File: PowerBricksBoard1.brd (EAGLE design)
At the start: 76.2 x 50.8 mm, 11 parts

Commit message: Board with draft routing
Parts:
- turned R1 to 270 degrees
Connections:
- net 12V renamed G
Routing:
- net ON/OFF: track 0.00 -> 58.2 mm
- net DATA: track 0.00 -> 31.6 mm
- net ALERT: track 0.00 -> 31.3 mm
- net CLK: track 0.00 -> 25.5 mm
- net G: track 0.00 -> 11.8 mm
- net 12_GND: track 0.00 -> 11.6 mm
- net N$1: track 0.00 -> 4.11 mm
- added copper zone on layer 1, net 12_GND
- added copper zone on layer 16, net 12_GND
- added copper zone on layer 16, net 48V
- added copper zone on layer 16, net 48_GND
- added copper zone on layer 1, net G
- added copper zone on layer 16, net G

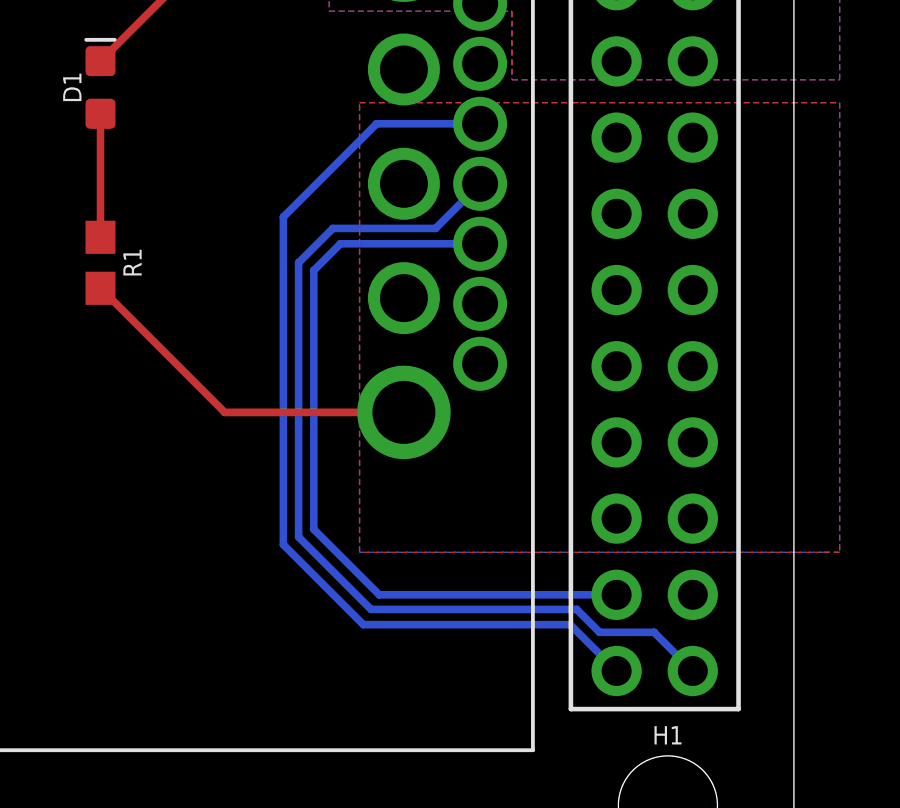
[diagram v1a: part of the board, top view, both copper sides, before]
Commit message: Fixed DRC error
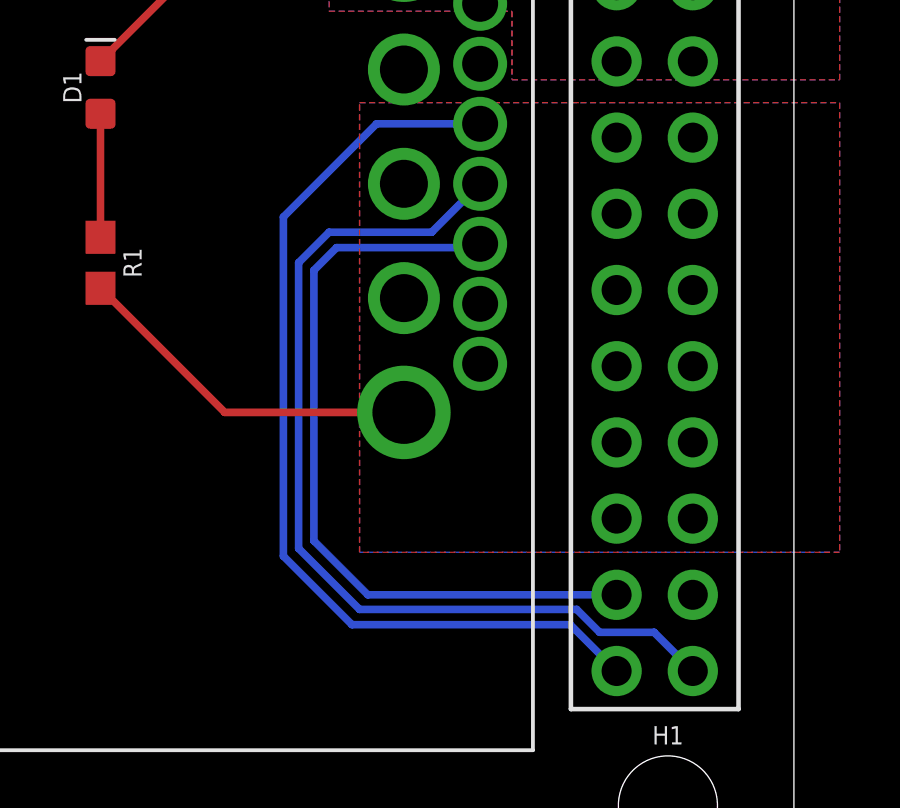
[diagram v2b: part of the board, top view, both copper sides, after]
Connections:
- removed net N$14: U$5.53
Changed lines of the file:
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@@
 <setting verticaltext="up"/>
 </settings>
-<grid distance="10" unitdist="mil" unit="mil" style="lines" multiple="1" display="yes" altdistance="5" altunitdist="mil" altunit="mil"/>
+<grid distance="5" unitdist="mil" unit="mil" style="lines" multiple="1" display="yes" altdistance="5" altunitdist="mil" altunit="mil"/>
 <layers>
 <layer number="1" name="Top" color="4" fill="1" visible="yes" active="yes"/>
@@
 </class>
 </classes>
-<designrules name="default">
+<designrules name="ECE_Senior_Design">
 <description language="de">&lt;b&gt;EAGLE Design Rules&lt;/b&gt;
 &lt;p&gt;
@@
 Einstellungen hier und speichern die Design Rules unter
 einem neuen Namen ab.</description>
-<description language="en">&lt;b&gt;EAGLE Design Rules&lt;/b&gt;
+<description language="en">&lt;b&gt;ECE 402/477 Design Rules Version 2&lt;/b&gt;
 &lt;p&gt;
-The default Design Rules have been set to cover
-a wide range of applications. Your particular design
-may have different requirements, so please make the
-necessary adjustments and save your customized
-design rules under a new name.</description>
+These are the design rules to use for Purdue University electrical and computer engineering senior design PCBs.
+&lt;/p&gt;
+&lt;p&gt;
+Please make sure your boards conform to these design rules.
+&lt;/p&gt;
+</description>
 <param name="layerSetup" value="(1*16)"/>
-<param name="mtCopper" value="0.035mm 0.035mm 0.035mm 0.035mm 0.035mm 0.035mm 0.035mm 0.035mm 0.035mm 0.035mm 0.035mm 0.035mm 0.035mm 0.035mm 0.035mm 0.035mm"/>
-<param name="mtIsolate" value="1.5mm 0.15mm 0.2mm 0.15mm 0.2mm 0.15mm 0.2mm 0.15mm 0.2mm 0.15mm 0.2mm 0.15mm 0.2mm 0.15mm 0.2mm"/>
-<param name="mdWireWire" value="6mil"/>
-<param name="mdWirePad" value="6mil"/>
-<param name="mdWireVia" value="6mil"/>
+<param name="mtCopper" value="0.0356mm 0.0356mm 0.0356mm 0.0356mm 0.0356mm 0.0356mm 0.0356mm 0.0356mm 0.0356mm 0.0356mm 0.0356mm 0.0356mm 0.0356mm 0.0356mm 0.0356mm 0.0356mm"/>
+<param name="mtIsolate" value="1.5011mm 0.1499mm 0.2007mm 0.1499mm 0.2007mm 0.1499mm 0.2007mm 0.1499mm 0.2007mm 0.1499mm 0.2007mm 0.1499mm 0.2007mm 0.1499mm 0.2007mm"/>
+<param name="mdWireWire" value="8mil"/>
+<param name="mdWirePad" value="8mil"/>
+<param name="mdWireVia" value="8mil"/>
 <param name="mdPadPad" value="6mil"/>
-<param name="mdPadVia" value="6mil"/>
-<param name="mdViaVia" value="6mil"/>
+<param name="mdPadVia" value="8mil"/>
+<param name="mdViaVia" value="8mil"/>
 <param name="mdSmdPad" value="6mil"/>
 <param name="mdSmdVia" value="6mil"/>
 <param name="mdSmdSmd" value="6mil"/>
-<param name="mdViaViaSameLayer" value="6mil"/>
+<param name="mdViaViaSameLayer" value="8mil"/>
 <param name="mnLayersViaInSmd" value="2"/>
-<param name="mdCopperDimension" value="40mil"/>
-<param name="mdDrill" value="6mil"/>
+<param name="mdCopperDimension" value="15mil"/>
+<param name="mdDrill" value="8mil"/>
 <param name="mdSmdStop" value="0mil"/>
-<param name="msWidth" value="6mil"/>
-<param name="msDrill" value="0.35mm"/>
-<param name="msMicroVia" value="9.99mm"/>
+<param name="msWidth" value="8mil"/>
+<param name="msDrill" value="13mil"/>
+<param name="msMicroVia" value="13mil"/>
 <param name="msBlindViaRatio" value="0.5"/>
 <param name="rvPadTop" value="0.25"/>
@@
 <param name="rvMicroViaOuter" value="0.25"/>
 <param name="rvMicroViaInner" value="0.25"/>
-<param name="rlMinPadTop" value="10mil"/>
+<param name="rlMinPadTop" value="7mil"/>
 <param name="rlMaxPadTop" value="20mil"/>
-<param name="rlMinPadInner" value="10mil"/>
+<param name="rlMinPadInner" value="7mil"/>
 <param name="rlMaxPadInner" value="20mil"/>
-<param name="rlMinPadBottom" value="10mil"/>
+<param name="rlMinPadBottom" value="7mil"/>
 <param name="rlMaxPadBottom" value="20mil"/>
-<param name="rlMinViaOuter" value="8mil"/>
+<param name="rlMinViaOuter" value="7mil"/>
 <param name="rlMaxViaOuter" value="20mil"/>
-<param name="rlMinViaInner" value="8mil"/>
+<param name="rlMinViaInner" value="7mil"/>
 <param name="rlMaxViaInner" value="20mil"/>
 <param name="rlMinMicroViaOuter" value="4mil"/>
@@
 <param name="mvStopFrame" value="1"/>
 <param name="mvCreamFrame" value="0"/>
-<param name="mlMinStopFrame" value="4mil"/>
-<param name="mlMaxStopFrame" value="4mil"/>
+<param name="mlMinStopFrame" value="3mil"/>
+<param name="mlMaxStopFrame" value="3mil"/>
 <param name="mlMinCreamFrame" value="0mil"/>
 <param name="mlMaxCreamFrame" value="0mil"/>
@@
 <contactref element="U$1" pad="SMBALERT"/>
 <contactref element="U$5" pad="55"/>
-<wire x1="65.74" y1="24.22" x2="64.253" y2="22.733" width="0.254" layer="16"/>
-<wire x1="59.69" y1="12.446" x2="62.103" y2="10.033" width="0.254" layer="16"/>
+<wire x1="65.74" y1="24.22" x2="64.126" y2="22.606" width="0.254" layer="16"/>
+<wire x1="59.69" y1="12.065" x2="61.722" y2="10.033" width="0.254" layer="16"/>
 <wire x1="68.961" y1="10.033" x2="69.723" y2="9.271" width="0.254" layer="16"/>
 <wire x1="71.539" y1="9.271" x2="72.83" y2="7.98" width="0.254" layer="16"/>
-<wire x1="64.253" y1="22.733" x2="60.833" y2="22.733" width="0.254" layer="16"/>
-<wire x1="60.833" y1="22.733" x2="59.69" y2="21.59" width="0.254" layer="16"/>
-<wire x1="59.69" y1="21.59" x2="59.69" y2="12.446" width="0.254" layer="16"/>
-<wire x1="62.103" y1="10.033" x2="68.961" y2="10.033" width="0.254" layer="16"/>
+<wire x1="64.126" y1="22.606" x2="60.706" y2="22.606" width="0.254" layer="16"/>
+<wire x1="60.706" y1="22.606" x2="59.69" y2="21.59" width="0.254" layer="16"/>
+<wire x1="59.69" y1="21.59" x2="59.69" y2="12.065" width="0.254" layer="16"/>
+<wire x1="61.722" y1="10.033" x2="68.961" y2="10.033" width="0.254" layer="16"/>
 <wire x1="69.723" y1="9.271" x2="71.539" y2="9.271" width="0.254" layer="16"/>
 </signal>
@@
 <wire x1="65.74" y1="26.22" x2="62.288" y2="26.22" width="0.254" layer="16"/>
 <wire x1="62.288" y1="26.22" x2="59.182" y2="23.114" width="0.254" layer="16"/>
-<wire x1="59.182" y1="23.114" x2="59.182" y2="12.192" width="0.254" layer="16"/>
-<wire x1="59.182" y1="12.192" x2="61.849" y2="9.525" width="0.254" layer="16"/>
+<wire x1="59.182" y1="23.114" x2="59.182" y2="11.811" width="0.254" layer="16"/>
+<wire x1="59.182" y1="11.811" x2="61.468" y2="9.525" width="0.254" layer="16"/>
 <wire x1="68.745" y1="9.525" x2="70.29" y2="7.98" width="0.254" layer="16"/>
-<wire x1="61.849" y1="9.525" x2="68.745" y2="9.525" width="0.254" layer="16"/>
+<wire x1="61.468" y1="9.525" x2="68.745" y2="9.525" width="0.254" layer="16"/>
 </signal>
 <signal name="CLK">
 <contactref element="U$1" pad="PMBCLK"/>
 <contactref element="U$5" pad="54"/>
-<wire x1="65.74" y1="22.22" x2="61.082" y2="22.22" width="0.254" layer="16"/>
-<wire x1="62.378" y1="10.52" x2="70.29" y2="10.52" width="0.254" layer="16"/>
-<wire x1="61.082" y1="22.22" x2="60.198" y2="21.336" width="0.254" layer="16"/>
-<wire x1="60.198" y1="21.336" x2="60.198" y2="12.7" width="0.254" layer="16"/>
-<wire x1="60.198" y1="12.7" x2="62.378" y2="10.52" width="0.254" layer="16"/>
+<wire x1="65.74" y1="22.22" x2="65.613" y2="22.093" width="0.254" layer="16"/>
+<wire x1="65.613" y1="22.093" x2="60.955" y2="22.093" width="0.254" layer="16"/>
+<wire x1="61.997" y1="10.52" x2="70.29" y2="10.52" width="0.254" layer="16"/>
+<wire x1="60.955" y1="22.093" x2="60.198" y2="21.336" width="0.254" layer="16"/>
+<wire x1="60.198" y1="21.336" x2="60.198" y2="12.319" width="0.254" layer="16"/>
+<wire x1="60.198" y1="12.319" x2="61.997" y2="10.52" width="0.254" layer="16"/>
 </signal>
 <signal name="N$1">
@@
 <wire x1="53.086" y1="26.555" x2="53.086" y2="22.44" width="0.254" layer="1"/>
 </signal>
-<signal name="N$14">
-<contactref element="U$5" pad="53"/>
-</signal>
 </signals>
